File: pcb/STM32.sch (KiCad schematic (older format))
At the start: 31 parts, among them J1 Conn_02x07_Odd_Even, X1 ABM8G

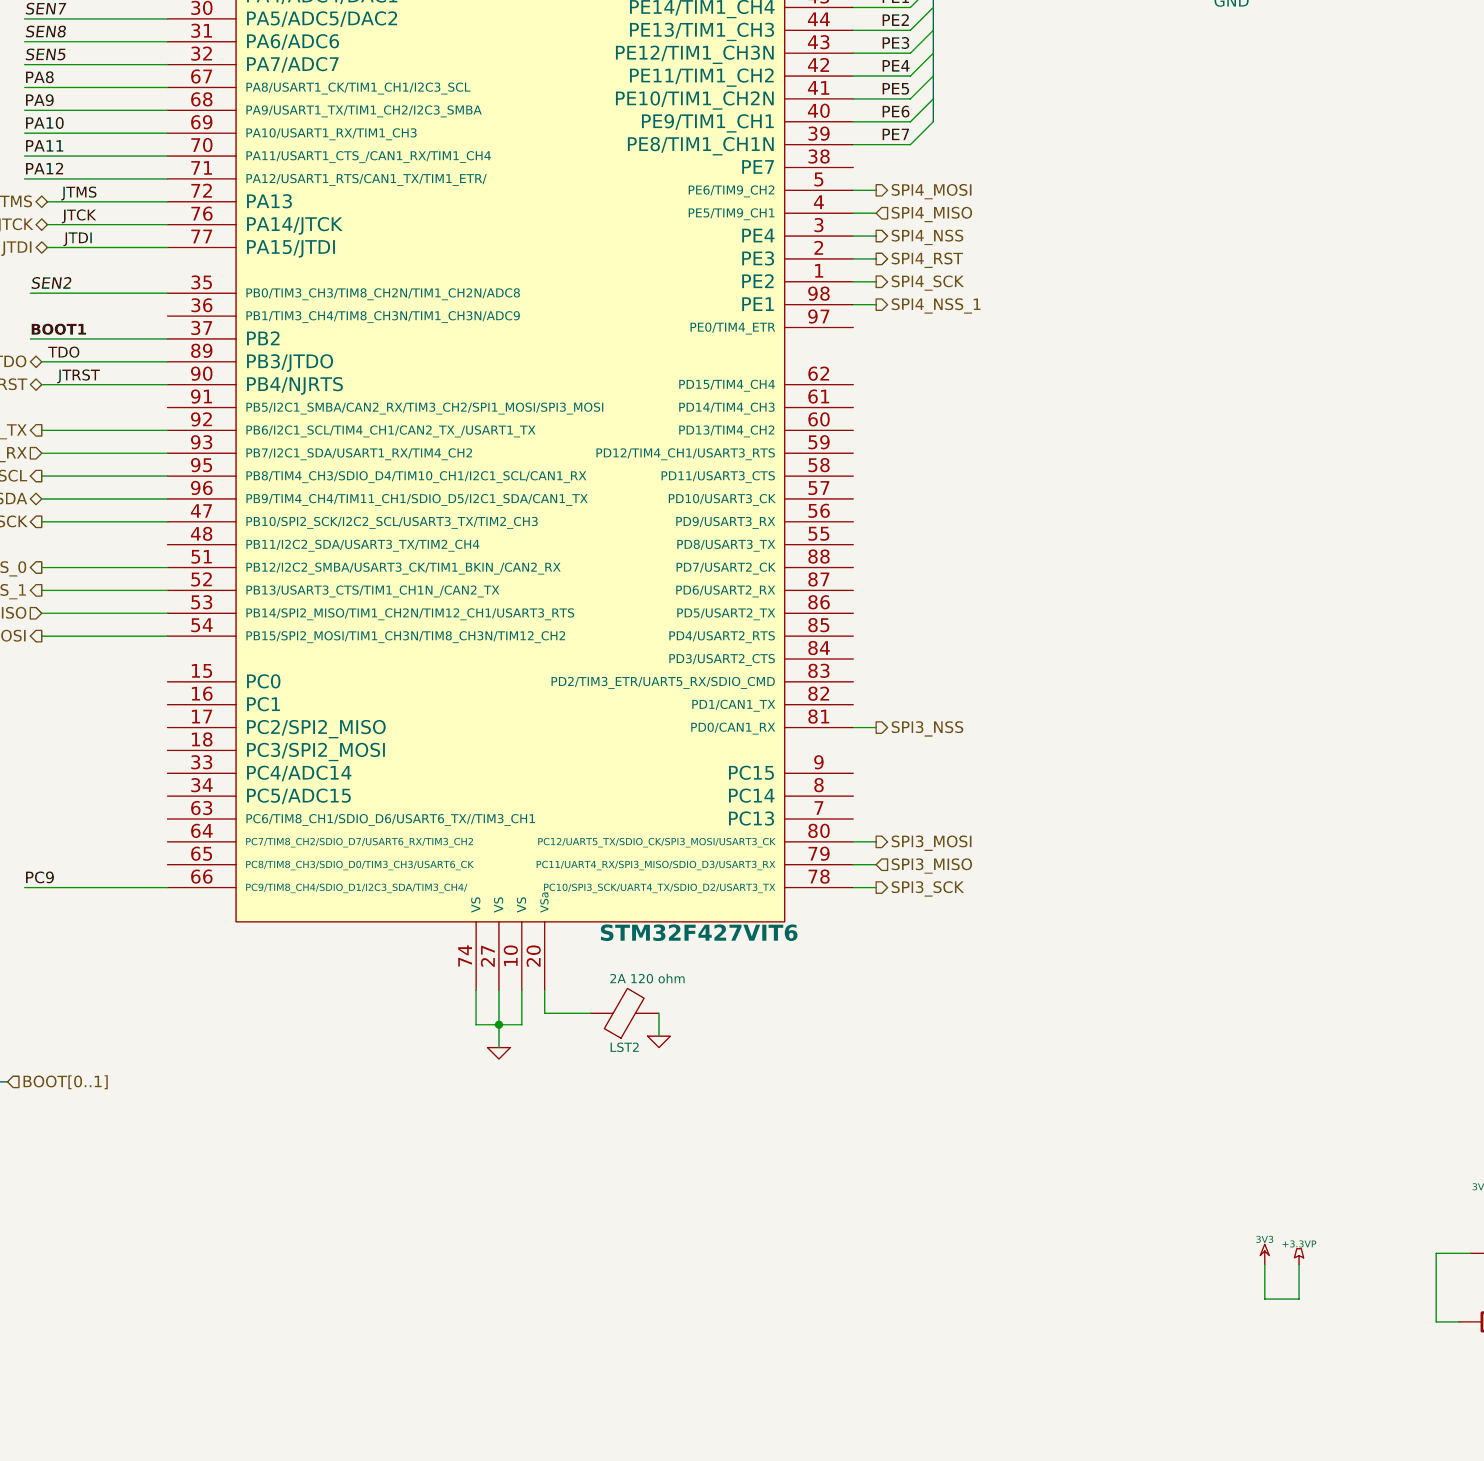
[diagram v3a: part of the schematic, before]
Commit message: Solved connections showed wrong by ERC
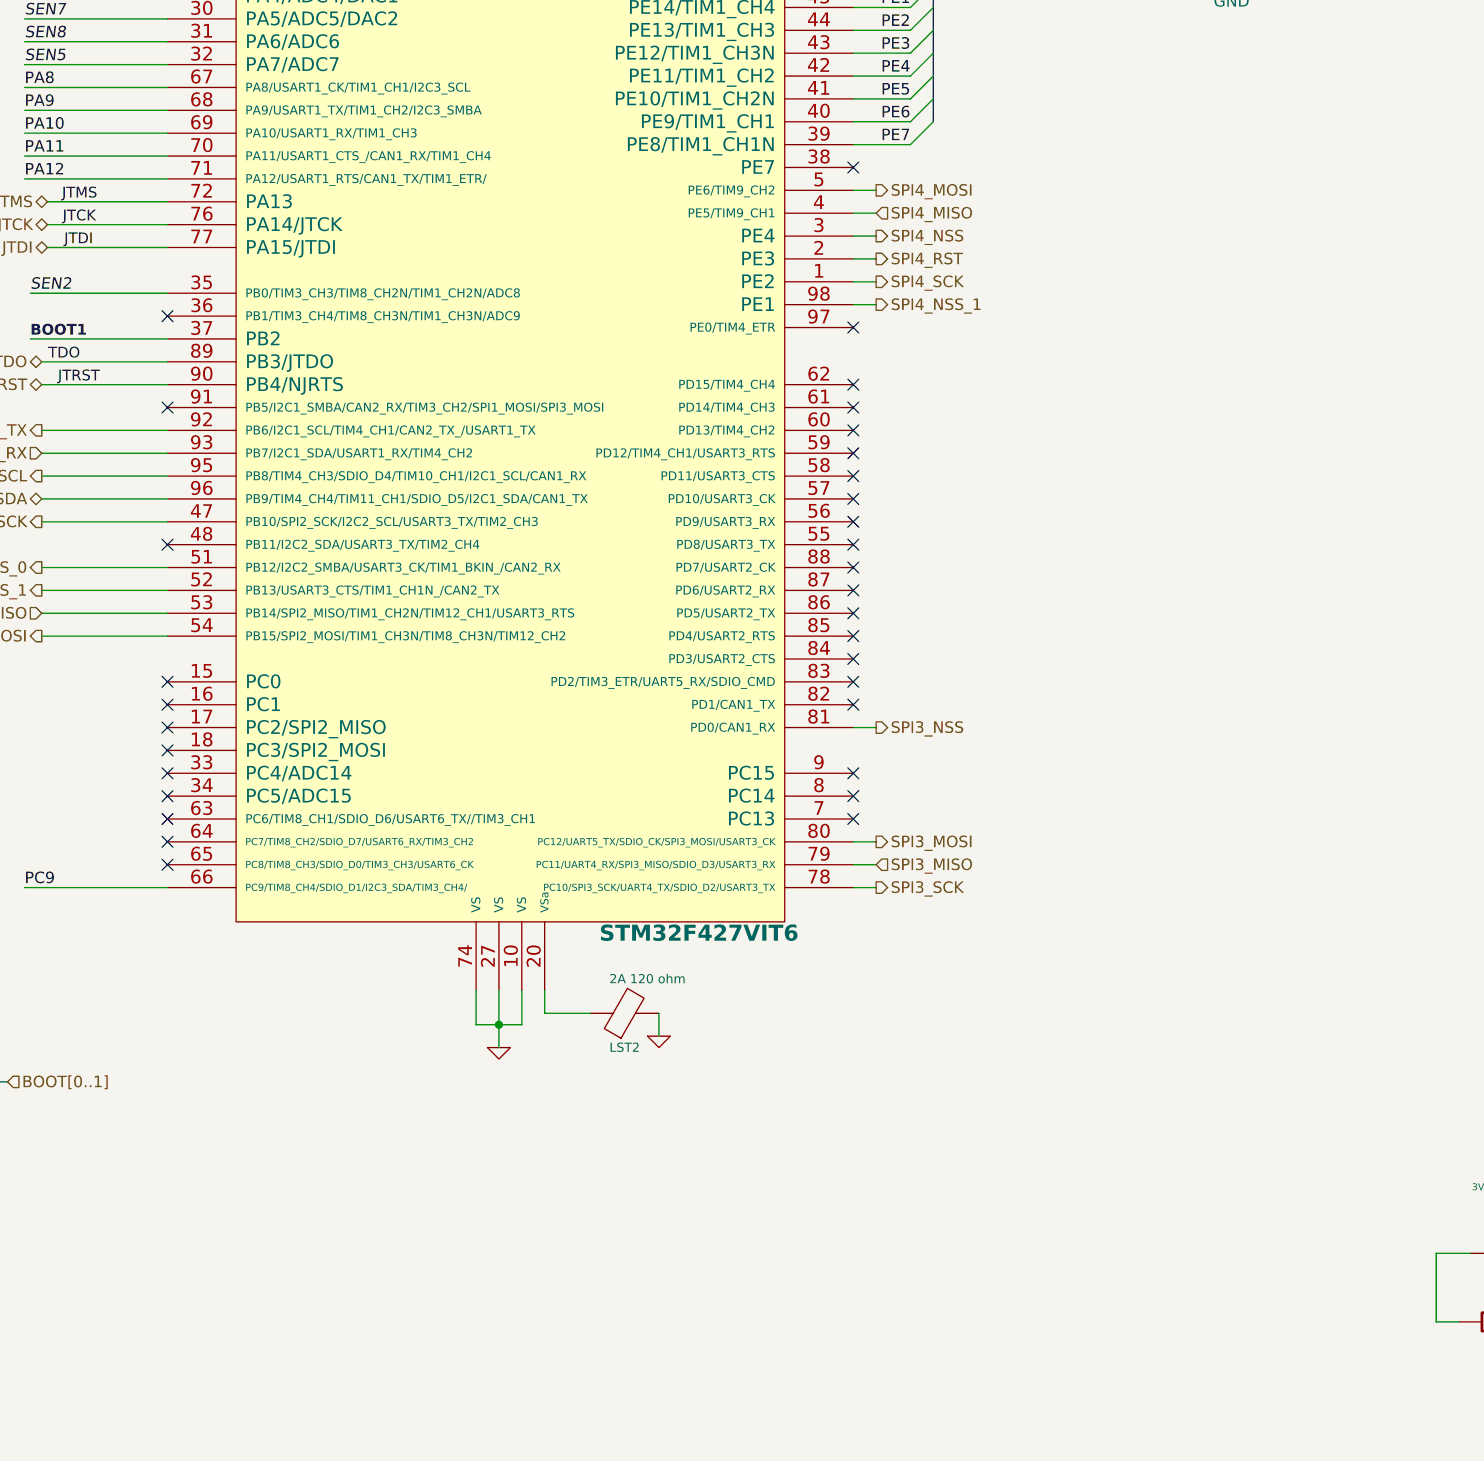
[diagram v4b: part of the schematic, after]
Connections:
- no-connect marks 0 -> 32
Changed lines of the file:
@@
 EESchema Schematic File Version 4
-LIBS:keep_breathing_ctrl-cache
 EELAYER 30 0
 EELAYER END
@@
 Comment4 ""
 $EndDescr
-$Comp
-L media_board:+3.3VP #PWR0121
-U 1 1 516D62A0
-P 7550 7750
-F 0 "#PWR0121" H 7600 7780 20  0001 C CNN
-F 1 "+3.3VP" H 7550 7840 30  0000 C CNN
-F 2 "" H 7550 7750 60  0001 C CNN
-F 3 "" H 7550 7750 60  0001 C CNN
-	1    7550 7750
-	1    0    0    -1
-$EndComp
 $Comp
 L ventilator-PowerSymbols:3V3_STM #PWR0122
@@
 $EndComp
 $Comp
-L ventilator-PowerSymbols:3V3_STM #PWR0149
-U 1 1 54556556
-P 900 650
-F 0 "#PWR0149" H 900 750 30  0001 C CNN
-F 1 "3V3_STM" H 900 760 30  0000 C CNN
-F 2 "" H 900 650 60  0001 C CNN
-F 3 "" H 900 650 60  0001 C CNN
-	1    900  650
-	1    0    0    -1
-$EndComp
-$Comp
 L Device:Ferrite_Bead LST1
 U 1 1 5455655C
@@
 $EndComp
 $Comp
-L media_board:3V3 #PWR0154
-U 1 1 54560F39
-P 7400 7750
-F 0 "#PWR0154" H 7400 7850 30  0001 C CNN
-F 1 "3V3" H 7400 7860 30  0000 C CNN
-F 2 "" H 7400 7750 60  0001 C CNN
-F 3 "" H 7400 7750 60  0001 C CNN
-	1    7400 7750
-	1    0    0    -1
-$EndComp
-$Comp
 L Device:C_Small CST3
 U 1 1 5456EF09
@@
 Wire Wire Line
 	8850 7500 8400 7500
-Wire Wire Line
-	7550 7750 7550 7900
 Connection ~ 4050 6700
 Wire Wire Line
@@
 	1300 7700 1300 7600
 Wire Wire Line
-	7400 7750 7400 7900
-Wire Wire Line
 	6200 1600 6200 1200
 Wire Wire Line
@@
 Wire Wire Line
 	2600 4400 2050 4400
-Wire Wire Line
-	7400 7900 7550 7900
 Wire Wire Line
 	4050 6700 4050 6800
@@
 Wire Wire Line
 	5700 3550 5600 3550
-Wire Bus Line
-	1800 6950 1800 7200
-Wire Bus Line
-	5950 2050 5950 2750
-Wire Bus Line
-	8950 1300 8950 2100
 $Comp
 L CSS-95B30-SMT:CSS-95B30-SMT LS1
@@
 	1    0    0    -1
 $EndComp
+$Comp
+L ventilator-PowerSymbols:3V3_STM #PWR0149
+U 1 1 54556556
+P 900 650
+F 0 "#PWR0149" H 900 750 30  0001 C CNN
+F 1 "3V3_STM" H 900 760 30  0000 C CNN
+F 2 "" H 900 650 60  0001 C CNN
+F 3 "" H 900 650 60  0001 C CNN
+	1    900  650
+	1    0    0    -1
+$EndComp
+NoConn ~ 5600 2950
+NoConn ~ 5600 3650
+NoConn ~ 5600 3900
+NoConn ~ 5600 4000
+NoConn ~ 5600 4100
+NoConn ~ 5600 4200
+NoConn ~ 5600 4300
+NoConn ~ 5600 4400
+NoConn ~ 5600 4500
+NoConn ~ 5600 4600
+NoConn ~ 5600 4700
+NoConn ~ 5600 4800
+NoConn ~ 5600 4900
+NoConn ~ 5600 5000
+NoConn ~ 5600 5100
+NoConn ~ 5600 5200
+NoConn ~ 5600 5300
+NoConn ~ 5600 5600
+NoConn ~ 5600 5700
+NoConn ~ 5600 5800
+NoConn ~ 2600 4600
+NoConn ~ 2600 5200
+NoConn ~ 2600 5300
+NoConn ~ 2600 5400
+NoConn ~ 2600 5500
+NoConn ~ 2600 5600
+NoConn ~ 2600 5700
+NoConn ~ 2600 5800
+NoConn ~ 2600 5900
+NoConn ~ 2600 6000
+NoConn ~ 2600 3600
+NoConn ~ 2600 4000
+Wire Bus Line
+	1800 6950 1800 7200
+Wire Bus Line
+	5950 2050 5950 2750
+Wire Bus Line
+	8950 1300 8950 2100
 $EndSCHEMATC
